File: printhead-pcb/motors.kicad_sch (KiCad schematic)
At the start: 1 part, among them J15 BreakoutBoardADXL345

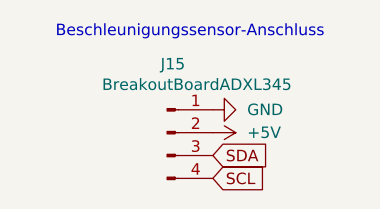
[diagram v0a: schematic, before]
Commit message: added complete list of components for i2c
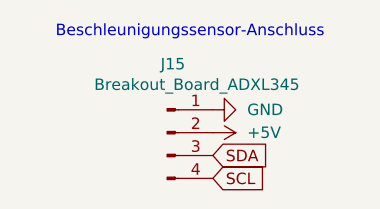
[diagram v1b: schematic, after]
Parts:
- J15: value BreakoutBoardADXL345 -> Breakout_Board_ADXL345
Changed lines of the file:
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@@
 			)
 		)
-		(property "Value" "BreakoutBoardADXL345"
+		(property "Value" "Breakout_Board_ADXL345"
 			(at 145.542 44.196 0)
 			(effects

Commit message: implemented custom footprint
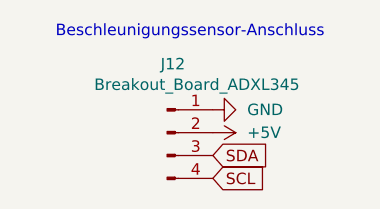
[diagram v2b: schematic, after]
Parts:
- renumbered J15 to J12
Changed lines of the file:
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@@
 		(on_board yes)
 		(dnp no)
-		(property "Reference" "J15"
+		(property "Reference" "J12"
 			(at 142.875 41.91 0)
 			(effects
@@
 			(project "printhead-pcb"
 				(path "/813ad687-b864-44a5-b729-c4edf26b731d/8c761283-af5f-48de-92da-23f77afbf455"
-					(reference "J15")
+					(reference "J12")
 					(unit 1)
 				)
